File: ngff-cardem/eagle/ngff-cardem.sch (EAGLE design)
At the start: 132 parts, among them IC201 CB3Q3244PW, IC202 CB3Q3244PW, IC203 IP4234CZ6, IC301 MCP1703CB, IC302 TPS22958-DGN, J301 PJ-002BH-SMT-TR, M2 MENTOR_12701001, M3 MENTOR_12701001, Q201 12MHz, T101 BC847, U201 IP4234CZ6, U202 AT91SAM3S-AU, U301 MIC5366-1.8YC5, X101 PINHD-2X4, X102 ZX360D-B-10P(30), X201 MINI-USB-SHIELD-UX60-MB-5ST, X202 2.54mm, X301 22-23-2041

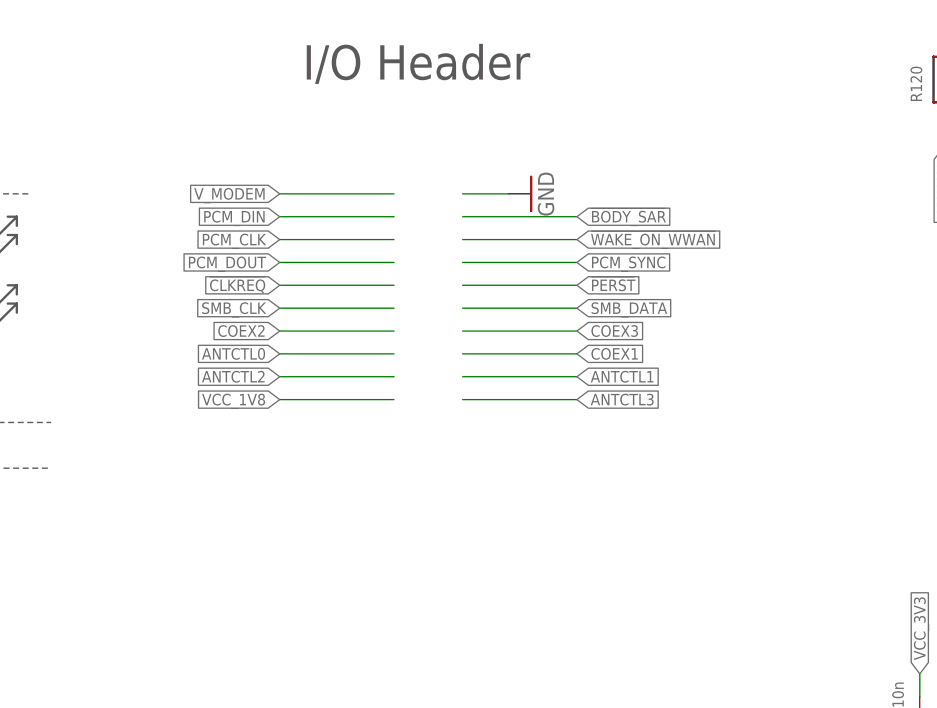
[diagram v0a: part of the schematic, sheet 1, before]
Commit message: add and route PCM header
Pin assignment according to QMOD based on EC20, EC25 and ME909 mapping
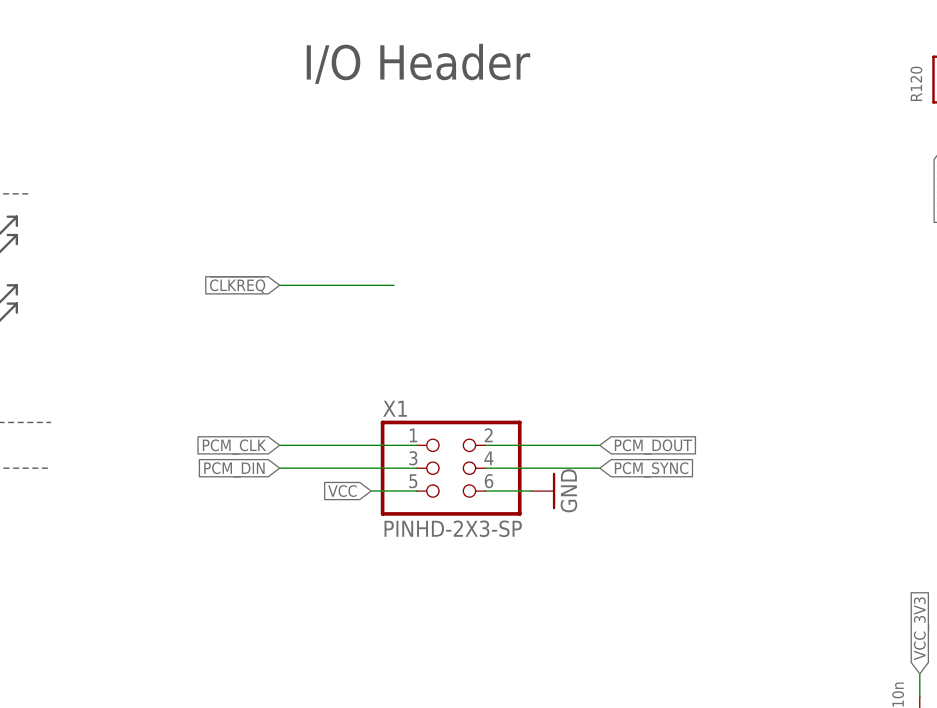
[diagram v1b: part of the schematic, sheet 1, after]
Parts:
- added R1: 10k, rc-sysmocom:RESISTOR_0603
- added TP1: TPTP14R, testpad:TPTP14R
- added X1: PINHD-2X3-SP, SparkFun-Connectors:PINHD-2X3
- C301: DESCRIPTION NO DESCRIPTION -> CAP ALUM 220UF 20%% 25V SMD; MANUFACTURER UNKNOWN MANUFACTURER -> Nichicon; MANUFACTURERPARTNUMBER UNKNOWN MANUFACTURER PART NUMBER -> UUD1E221MNL1GS; ROHSCERTIFICATE UNKNOWN ROHS CERTIFICATE -> RoHS3-konform; SOURCE UNKNOWN SOURCE -> DIGIKEY; SOURCEPARTNUMBER UNKNOWN SOURCE PART NUMBER -> 493-2278-1-ND
- IC302: CLASS UNKNOWN CLASS -> IC; DESCRIPTION NO DESCRIPTION -> IC PWR SWITCH N-CHAN 1:1 8MSOP; MANUFACTURER UNKNOWN MANUFACTURER -> Texas Instruments; MANUFACTURERPARTNUMBER UNKNOWN MANUFACTURER PART NUMBER -> TPS22958DGNR; ROHSCERTIFICATE UNKNOWN ROHS CERTIFICATE -> RoHS3-konform; SOURCE UNKNOWN SOURCE -> DIGIKEY; SOURCEPARTNUMBER UNKNOWN SOURCE PART NUMBER -> 296-47367-1-ND
- U201, X201: DESCRIPTION NO DESCRIPTION -> (none); MANUFACTURER UNKNOWN MANUFACTURER -> (none); MANUFACTURERPARTNUMBER UNKNOWN MANUFACTURER PART NUMBER -> (none); ROHSCERTIFICATE UNKNOWN ROHS CERTIFICATE -> (none); SOURCEPARTNUMBER UNKNOWN SOURCE PART NUMBER -> (none)
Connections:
- new net N$5: IC201-CTL/PWR.!1OE
- new net VCC: X1.5
- net ERASE: now also TP1.TP
- net GND: now also R1.1, X1.6
- net MODEM_EN: now also R1.2
- net N$9: now also X201S.S1, X201S.S4
- net PCM_CLK: now also X1.1
- net PCM_DIN: now also X1.3
- net PCM_DOUT: now also X1.2
- net PCM_SYNC: now also X1.4

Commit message: ngff-cardem: reduce number of options jumper to 3
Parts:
- removed X101: PINHD-2X4, laforge:PINHD-2X4
- added X2: PINHD-2X3-SP, SparkFun-Connectors:PINHD-2X3
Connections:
- net !GPS_DISABLE: now also X2.5; no longer X101.5
- net !NGFF_RESET: no longer X101.7
- net !W_DISABLE: now also X2.3; no longer X101.3
- net GND: now also X2.4, X2.6; no longer X101.4, X101.6, X101.8
- net N$21: now also X2.2; no longer X101.2
- net PWR_ON: now also X2.1; no longer X101.1
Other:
- moved on the sheet: LED1, NGFF101G$1, R102, R103, R104, R105, R106, R107, R108, R109, R110, R111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

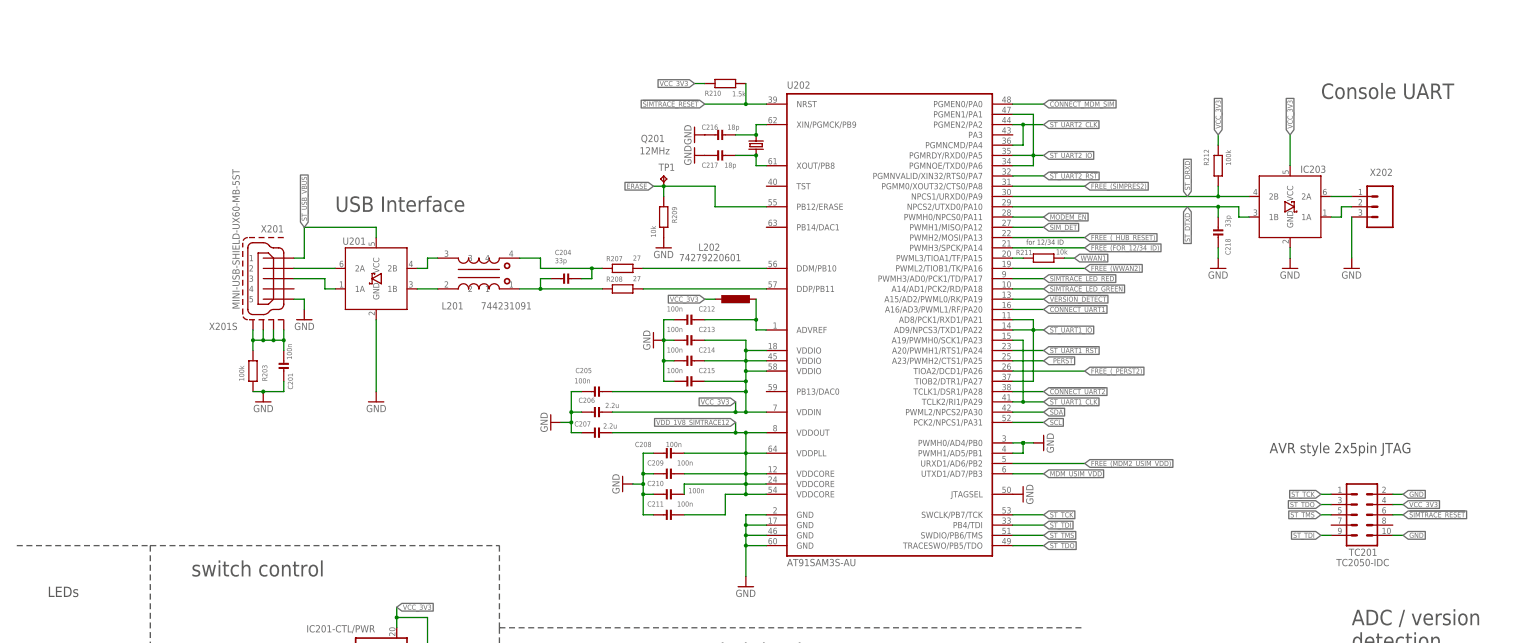
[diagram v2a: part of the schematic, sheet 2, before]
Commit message: ngff-cardem: add PRW_ON logic
PU to V_MODEM, and a TUN inverter to GPIO (PA26), so get "default on,
but with ability for software to override should it ever be needed".
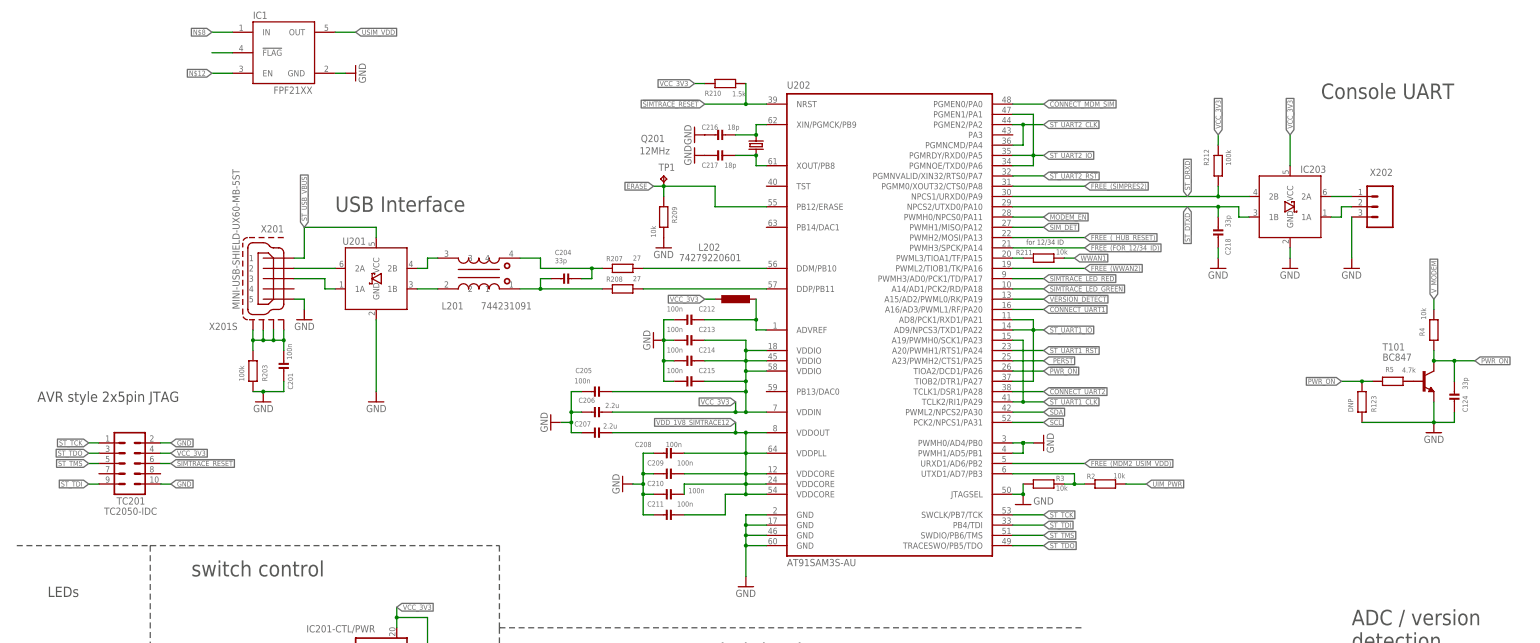
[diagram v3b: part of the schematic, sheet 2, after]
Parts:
- removed R121: DNP, rc-sysmocom:RESISTOR_0603
- removed R122: 4.42k, rc-sysmocom:RESISTOR_0603
- added IC1: FPF21XX, FPF2109:FPF21XX
- added R2, R3, R4: 10k, rc-sysmocom:RESISTOR_0603
- added R5: 4.7k, rc-sysmocom:RESISTOR_0603
- X1, X2: ROHSCERTIFICATE UNKNOWN ROHS CERTIFICATE -> RoHS3-konform
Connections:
- removed net DCDC_ENA: DCDC301.ON/OFF
- removed net FREE_(_PERST2): U202.TIOA2/DCD1/PA26
- removed net MDM_USIM_VDD: U202.UTXD1/AD7/PB3
- removed net N$39: R122.2, T101.B
- removed net PERST1: C124.1, R121.2, T101.C
- new net !PWR_ON: R123.1, R5.2, U202.TIOA2/DCD1/PA26
- new net N$11: IC1.!FLAG
- new net N$12: IC1.EN
- new net N$14: R5.1, T101.B
- new net N$18: R2.1, R3.2, U202.UTXD1/AD7/PB3
- new net N$8: IC1.IN
- new net UIM_PWR: NGFF101G$1.UIM_PWR, R2.2
- net +VIN_PROT: now also DCDC301.ON/OFF
- net GND: now also IC1.GND, R3.1
- net PWR_ON: now also C124.1, R4.2, T101.C
- net USIM_VDD: now also IC1.OUT
- net VCC_1V8: no longer R103.2
- net VCC_3V3: no longer R121.1
- net V_MODEM: now also R4.1
- net _PERST: no longer R122.1, R123.1
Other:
- moved on the sheet: C303, R117, TC201

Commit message: ngff-cardem: add SIM Vcc switch logic
... consisting of two FPF2109 and a Schottky diode. Needs two GPIOs,
PU and PD for default "modem gives SIM pwr".
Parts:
- added D6: CUS08F30,H3F, diodes-sysmocom:DIODE-SCHOTTKY-SOD-323
- added IC2: FPF2109, FPF2109:FPF21XX
- added R6, R7: 10k, rc-sysmocom:RESISTOR_0603
- DCDC301: DESCRIPTION NO DESCRIPTION -> DC DC CONVERTER 0.6-5.5V 16.5W; LINK UNKNOWN LINK -> https://www.digikey.de/product-detail/de/abb-power-electron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; MANUFACTURER UNKNOWN MANUFACTURER -> ABB Power Electronics Inc.; MANUFACTURERPARTNUMBER UNKNOWN MANUFACTURER PART NUMBER -> PVX003A0X3-SRZ; ROHSCERTIFICATE UNKNOWN ROHS CERTIFICATE -> RoHS-konform; SOURCE UNKNOWN SOURCE -> DIGIKEY; SOURCEPARTNUMBER UNKNOWN SOURCE PART NUMBER -> 555-1264-1-ND
- IC1: value FPF21XX -> FPF2109; CLASS (none) -> IC; DESCRIPTION (none) -> IC PWR SWITCH P-CHAN 1:1 SOT23-5; LINK (none) -> https://www.digikey.de/product-detail/de/on-semiconductor/F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; MANUFACTURER (none) -> ON Semiconductor; MANUFACTURERPARTNUMBER (none) -> FPF2109; POPULATED (none) -> TRUE; ROHSCERTIFICATE (none) -> RoHS3-konform; SOURCE (none) -> DIGIKEY; SOURCEPARTNUMBER (none) -> FPF2109CT-ND
- IC203: CLASS DIODE -> TVS ARRAY; DESCRIPTION TVS DIODE 5.5V 6TSOP -> TVS DIODE 5.5VWM 6TSOP; LINK https://www.digikey.de/product-detail/de/IP4234CZ6,115/1727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 -> https://www.digikey.de/product-detail/de/nexperia-usa-inc/I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
- SIM101: DESCRIPTION NO DESCRIPTION -> CONN SIM CARD PUSH-PUSH R/A SMD; LINK UNKNOWN LINK -> https://www.digikey.de/product-detail/de/molex/0475530001/W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; MANUFACTURER UNKNOWN MANUFACTURER -> Molex; MANUFACTURERPARTNUMBER UNKNOWN MANUFACTURER PART NUMBER -> 0475530001; ROHSCERTIFICATE UNKNOWN ROHS CERTIFICATE -> RoHS3-konform; SOURCE UNKNOWN SOURCE -> DIGIKEY; SOURCEPARTNUMBER UNKNOWN SOURCE PART NUMBER -> WM3293TR-ND
- TP1: CLASS (none) -> UNKNOWN CLASS; DESCRIPTION (none) -> NO DESCRIPTION; LINK (none) -> UNKNOWN LINK; MANUFACTURER (none) -> UNKNOWN MANUFACTURER; MANUFACTURERPARTNUMBER (none) -> UNKNOWN MANUFACTURER PART NUMBER; POPULATED (none) -> TRUE; ROHSCERTIFICATE (none) -> UNKNOWN ROHS CERTIFICATE; SOURCE (none) -> UNKNOWN SOURCE; SOURCEPARTNUMBER (none) -> UNKNOWN SOURCE PART NUMBER
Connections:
- removed net ANTCTL0: NGFF101G$1.ANTCTL0
- removed net ANTCTL1: NGFF101G$1.ANTCTL1
- removed net ANTCTL2: NGFF101G$1.ANTCTL2
- removed net ANTCTL3: NGFF101G$1.ANTCTL3
- removed net COEX1: NGFF101G$1.COEX1
- removed net COEX2: NGFF101G$1.COEX2
- removed net COEX3: NGFF101G$1.COEX3
- removed net FREE_(MDM2_USIM_VDD): U202.URXD1/AD6/PB2
- removed net FREE_(WWAN2): U202.PWML2/TIOB1/TK/PA16
- removed net N$11: IC1.!FLAG
- removed net N$12: IC1.EN
- removed net N$8: IC1.IN
- removed net SMB_CLK: NGFF101G$1.I2C_SCL_SIWI
- removed net SMB_DATA: NGFF101G$1.I2C_SDA_SIWI
- removed net _!USIM2_RESET: NGFF101G$1.SYSCLK_HW/UIM2_RESET_SIWI
- removed net _SIM2_DET: NGFF101G$1.I2C_SCL_HW/SIM_DET2_SIWI
- removed net _USIM2_CLK: NGFF101G$1.I2C_IRQ_HW/UIM2_CLK_SIWI
- removed net _USIM2_DATA: NGFF101G$1.I2C_SDA_HW/UIM2_DATA_SIWI
- removed net _USIM2_POWER: NGFF101G$1.TX_BLANKING_HW/UIM2_PWR_SIWI
- new net EN_MDM_SIM_VDD: IC2.EN, R6.1, U202.PWML2/TIOB1/TK/PA16
- new net EN_ST_SIM_VDD): IC1.EN, R7.1, U202.URXD1/AD6/PB2
- new net N$19: D6.A, IC1.OUT
- net GND: now also IC2.GND, R7.2
- net UIM_PWR: now also IC2.IN
- net USIM_VDD: now also D6.C, IC2.OUT; no longer IC1.OUT
- net VCC_3V3: now also IC1.IN, R6.2
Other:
- note added: "PWR_ON logic"
- note added: "SIM Vcc switches"
- moved on the sheet: C124, C201, C204, C205, C206, C207, C208, C209, C210, C211, C212, C213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

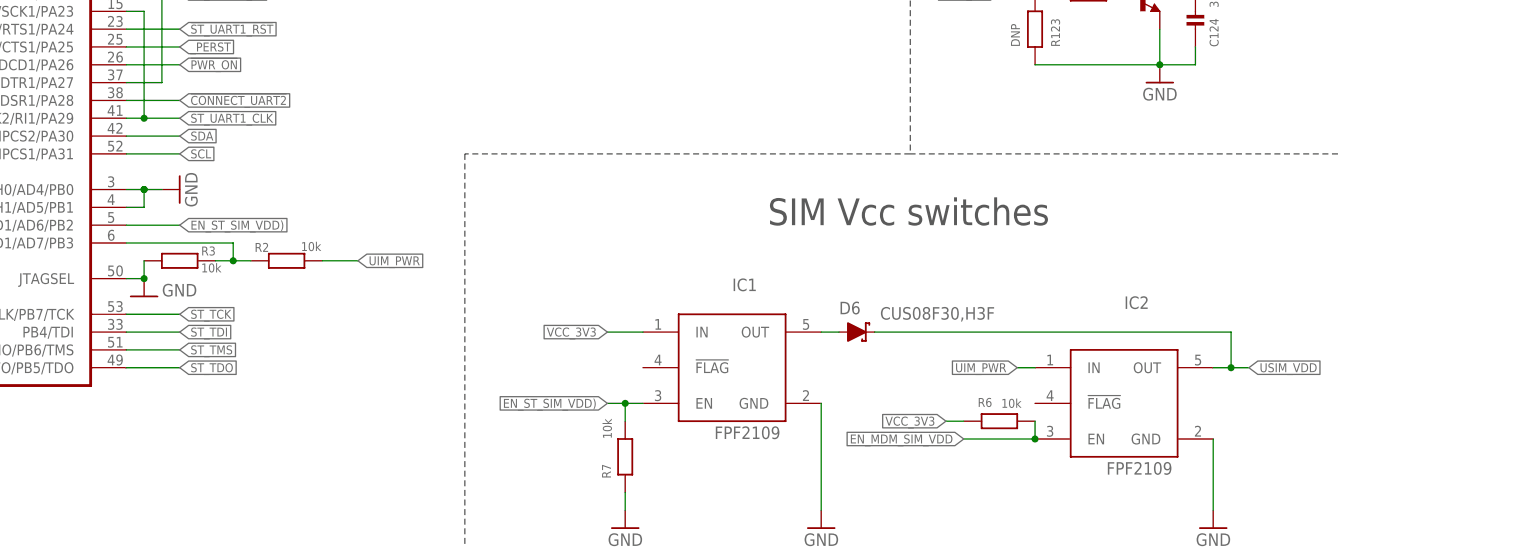
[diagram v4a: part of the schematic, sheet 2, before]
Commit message: ngff-cardem: use 30k/47k voltage divider for UIM_PWR like in octsimtest
solves SYS#5475
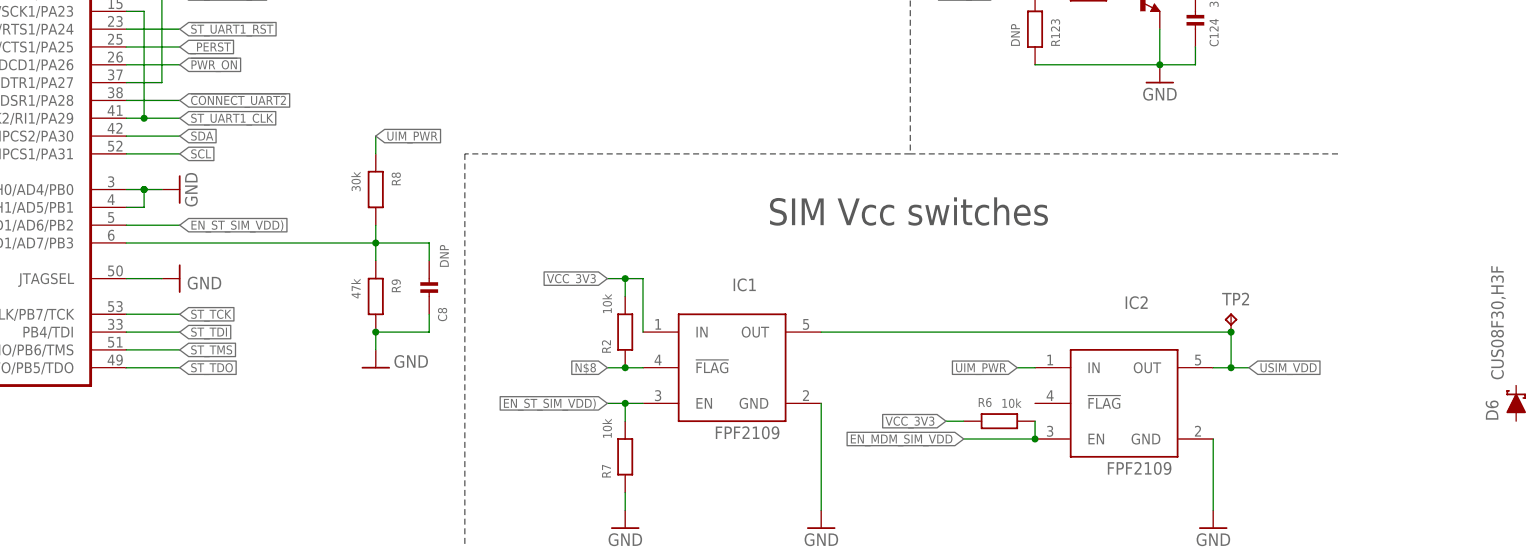
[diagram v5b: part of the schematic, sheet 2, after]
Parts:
- removed R3: 10k, rc-sysmocom:RESISTOR_0603
- added C8: DNP, rc-sysmocom:CAP_CERAMIC_0603
- added R8: 30k, rc-sysmocom:RESISTOR_0603
- added R9: 47k, rc-sysmocom:RESISTOR_0603
- added TP2: TPTP14R, testpad:TPTP14R
- R2: DESCRIPTION RES 10K OHM 1%% 1/10W 0603 -> RES 10K OHM 1%% 1/8W 0603; LINK https://www.digikey.de/product-detail/de/stackpole-electronics-inc/RMCF0603FT10K0/RMCF0603FT10K0CT-ND -> https://www.digikey.de/product-detail/de/stackpole-electronics-inc/RNCP0603FTD10K0/RNCP0603FTD10K0CT-ND; MANUFACTURERPARTNUMBER YPE HTML PUBLIC -> RNCP0603FTD10K0; ROHSCERTIFICATE Bleifrei / RoHS3-konform -> RoHS3-konform; SOURCEPARTNUMBER RMCF0603FT10K0CT-ND -> RNCP0603FTD10K0CT-ND
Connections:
- removed net N$19: D6.A, IC1.OUT
- new net N$8: IC1.!FLAG, R2.2
- net GND: now also C8.2, R9.1; no longer R3.1
- net N$18: now also C8.1, R8.1, R9.2; no longer R2.1, R3.2
- net UIM_PWR: now also R8.2; no longer R2.2
- net USIM_VDD: now also IC1.OUT, TP2.TP; no longer D6.C
- net VCC_3V3: now also R2.1
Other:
- moved on the sheet: D6, R2
